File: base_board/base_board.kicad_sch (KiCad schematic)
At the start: 53 parts, among them J1 Conn_ARM_JTAG_SWD_20, SW1 SW_Push, U1 STM32F446ZEJx, U2 IS42S16400J-xT, U3 BMI270, U4 USB_C_Receptacle_USB2.0, U5 10p, U6 10p, U7 LD3985M33R_SOT23, Y1 Crystal_GND24

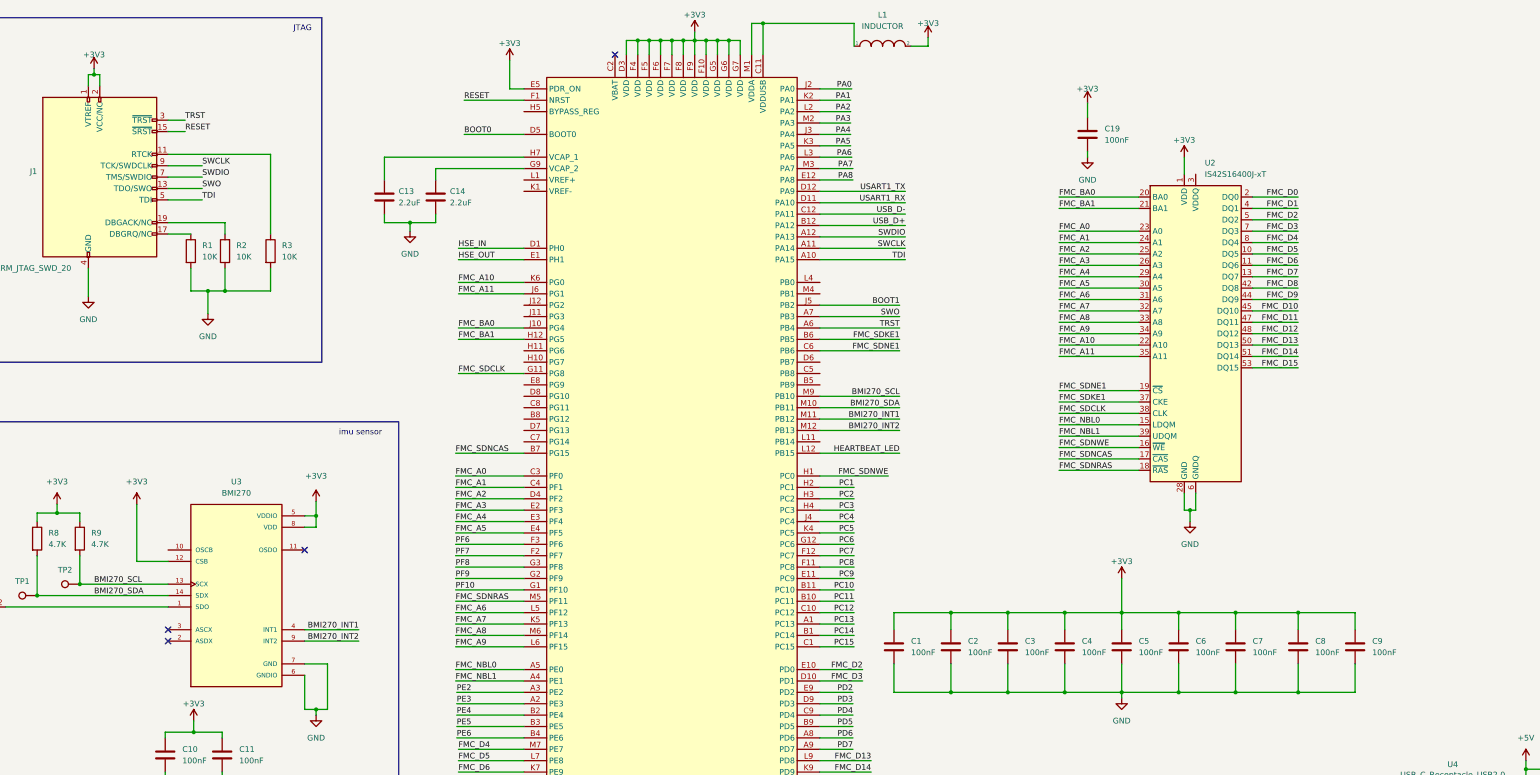
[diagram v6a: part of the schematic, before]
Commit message: [pcb] completed routing except VDDUSB
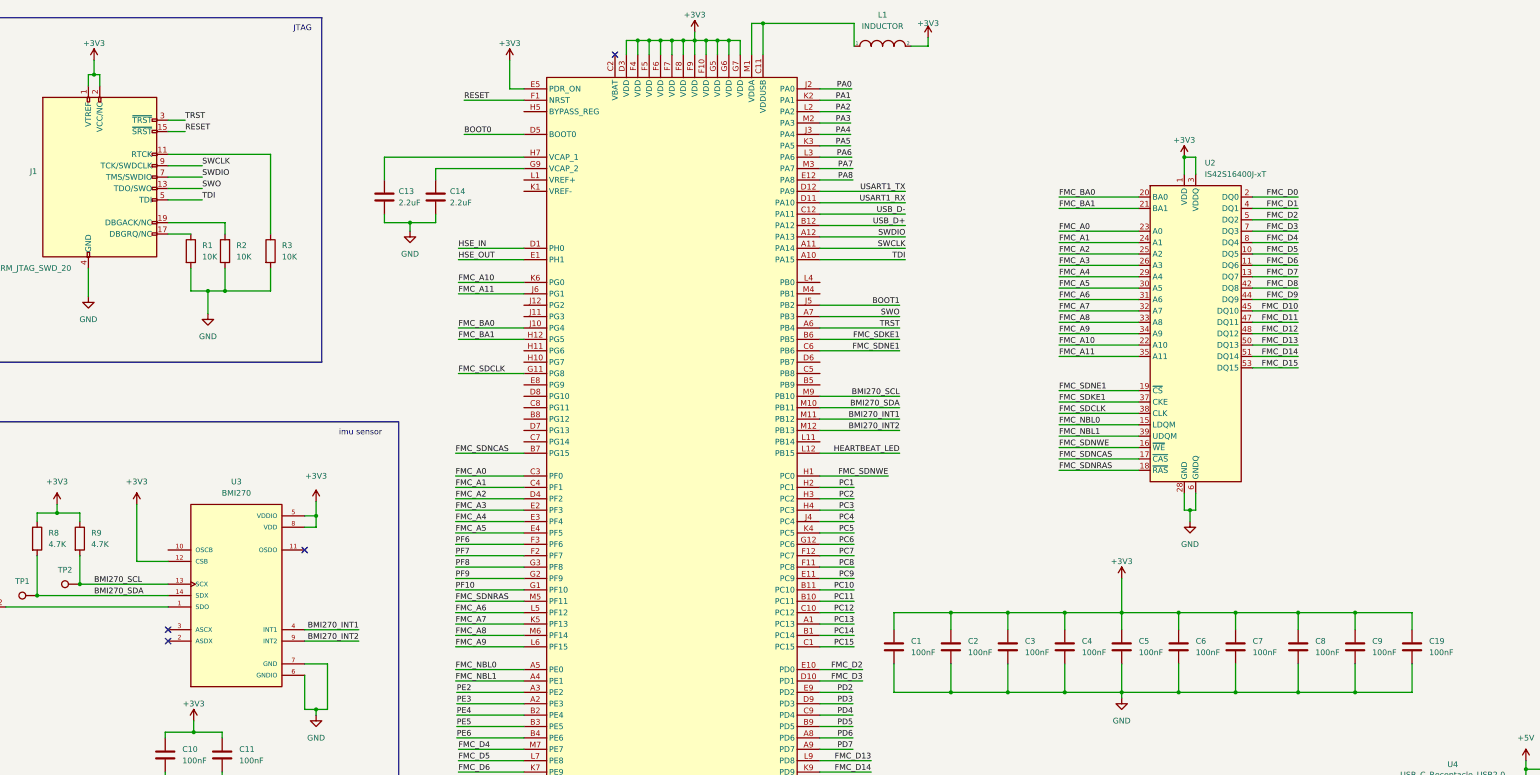
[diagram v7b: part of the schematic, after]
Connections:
- net +3.3V is gone; now on net +3V3: J1.1 (VTREF), J1.2 (VCC/NC)
- net +3V3: now also U2.3 (VDDQ), U2.43 (VDDQ), U2.49 (VDDQ), U2.9 (VDDQ)
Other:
- moved on the sheet: C19
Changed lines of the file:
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@@
   (junction (at 58.42 255.905) (diameter 0) (color 0 0 0 0)
   )
+  (junction (at 323.85 165.1) (diameter 0) (color 0 0 0 0)
+  )
   (junction (at 361.95 182.245) (diameter 0) (color 0 0 0 0)
   )
@@
   (junction (at 297.18 147.32) (diameter 0) (color 0 0 0 0)
   )
+  (junction (at 323.85 147.32) (diameter 0) (color 0 0 0 0)
+  )
   (junction (at 259.08 165.1) (diameter 0) (color 0 0 0 0)
   )
@@
   (junction (at 179.07 209.55) (diameter 0) (color 0 0 0 0)
   )
+  (junction (at 285.75 45.72) (diameter 0) (color 0 0 0 0)
+  )
   (junction (at 175.26 209.55) (diameter 0) (color 0 0 0 0)
   )
@@
     (stroke (width 0) (type default))
   )
+  (wire (pts (xy 336.55 147.32) (xy 323.85 147.32))
+    (stroke (width 0) (type default))
+  )
   (wire (pts (xy 259.08 147.32) (xy 246.38 147.32))
     (stroke (width 0) (type default))
@@
     (stroke (width 0) (type default))
   )
+  (wire (pts (xy 288.29 49.53) (xy 288.29 45.72))
+    (stroke (width 0) (type default))
+  )
   (wire (pts (xy 259.08 165.1) (xy 271.78 165.1))
     (stroke (width 0) (type default))
@@
     (stroke (width 0) (type default))
   )
+  (wire (pts (xy 336.55 165.1) (xy 323.85 165.1))
+    (stroke (width 0) (type default))
+  )
   (wire (pts (xy 123.19 132.08) (xy 138.43 132.08))
     (stroke (width 0) (type default))
@@
     (stroke (width 0) (type default))
   )
-  (wire (pts (xy 42.545 26.035) (xy 42.545 27.305))
+  (wire (pts (xy 42.545 24.13) (xy 42.545 27.305))
     (stroke (width 0) (type default))
   )
@@
     (stroke (width 0) (type default))
   )
+  (wire (pts (xy 336.55 151.13) (xy 336.55 147.32))
+    (stroke (width 0) (type default))
+  )
   (wire (pts (xy 89.535 128.27) (xy 92.075 128.27))
     (stroke (width 0) (type default))
@@
     (stroke (width 0) (type default))
   )
-  (wire (pts (xy 264.16 44.45) (xy 264.16 45.72))
-    (stroke (width 0) (type default))
-  )
   (wire (pts (xy 181.61 209.55) (xy 184.15 209.55))
     (stroke (width 0) (type default))
@@
     (stroke (width 0) (type default))
   )
+  (wire (pts (xy 336.55 158.75) (xy 336.55 165.1))
+    (stroke (width 0) (type default))
+  )
   (wire (pts (xy 300.99 59.69) (xy 311.15 59.69))
     (stroke (width 0) (type default))
@@
     (stroke (width 0) (type default))
   )
-  (wire (pts (xy 264.16 33.655) (xy 264.16 36.83))
-    (stroke (width 0) (type default))
-  )
   (wire (pts (xy 52.07 123.19) (xy 52.07 135.89))
     (stroke (width 0) (type default))
@@
     (stroke (width 0) (type default))
   )
+  (wire (pts (xy 285.75 45.72) (xy 288.29 45.72))
+    (stroke (width 0) (type default))
+  )
   (wire (pts (xy 204.47 88.9) (xy 222.25 88.9))
     (stroke (width 0) (type default))
@@
     )
   )
+  (symbol (lib_name "+3V3_7") (lib_id "power:+3V3") (at 42.545 24.13 0) (unit 1)
+    (in_bom yes) (on_board yes) (dnp no) (fields_autoplaced)
+    (property "Reference" "#PWR06" (at 42.545 27.94 0)
+      (effects (font (size 1.27 1.27)) hide)
+    )
+    (property "Value" "+3V3" (at 42.545 20.32 0)
+      (effects (font (size 1.27 1.27)))
+    )
+    (property "Footprint" "" (at 42.545 24.13 0)
+      (effects (font (size 1.27 1.27)) hide)
+    )
+    (property "Datasheet" "" (at 42.545 24.13 0)
+      (effects (font (size 1.27 1.27)) hide)
+    )
+    (pin "1")
+    (instances
+      (project "base_board"
+        (path "/2307506f-1d7e-4fdb-b101-b9905788fe29"
+          (reference "#PWR06") (unit 1)
+        )
+      )
+    )
+  )
   (symbol (lib_id "Device:R") (at 64.135 66.675 0) (unit 1)
     (in_bom yes) (on_board yes) (dnp no) (fields_autoplaced)
@@
     )
   )
-  (symbol (lib_id "power:+3.3V") (at 42.545 26.035 0) (unit 1)
-    (in_bom yes) (on_board yes) (dnp no) (fields_autoplaced)
-    (property "Reference" "#PWR0103" (at 42.545 29.845 0)
-      (effects (font (size 1.27 1.27)) hide)
-    )
-    (property "Value" "+3V3" (at 42.545 22.86 0)
-      (effects (font (size 1.27 1.27)))
-    )
-    (property "Footprint" "" (at 42.545 26.035 0)
-      (effects (font (size 1.27 1.27)) hide)
-    )
-    (property "Datasheet" "" (at 42.545 26.035 0)
-      (effects (font (size 1.27 1.27)) hide)
-    )
-    (pin "1")
-    (instances
-      (project "base_board"
-        (path "/2307506f-1d7e-4fdb-b101-b9905788fe29"
-          (reference "#PWR0103") (unit 1)
-        )
-      )
-    )
-  )
   (symbol (lib_id "Device:C") (at 27.94 222.885 0) (unit 1)
     (in_bom yes) (on_board yes) (dnp no) (fields_autoplaced)
@@
     )
   )
-  (symbol (lib_name "+3V3_6") (lib_id "power:+3V3") (at 264.16 33.655 0) (unit 1)
-    (in_bom yes) (on_board yes) (dnp no) (fields_autoplaced)
-    (property "Reference" "#PWR06" (at 264.16 37.465 0)
-      (effects (font (size 1.27 1.27)) hide)
-    )
-    (property "Value" "+3V3" (at 264.16 30.48 0)
-      (effects (font (size 1.27 1.27)))
-    )
-    (property "Footprint" "" (at 264.16 33.655 0)
-      (effects (font (size 1.27 1.27)) hide)
-    )
-    (property "Datasheet" "" (at 264.16 33.655 0)
-      (effects (font (size 1.27 1.27)) hide)
-    )
-    (pin "1")
-    (instances
-      (project "base_board"
-        (path "/2307506f-1d7e-4fdb-b101-b9905788fe29"
-          (reference "#PWR06") (unit 1)
-        )
-      )
-    )
-  )
   (symbol (lib_id "power:+3V3") (at 58.42 245.745 0) (unit 1)
     (in_bom yes) (on_board yes) (dnp no) (fields_autoplaced)
@@
     )
   )
-  (symbol (lib_name "GND_1") (lib_id "power:GND") (at 264.16 45.72 0) (mirror y) (unit 1)
-    (in_bom yes) (on_board yes) (dnp no)
-    (property "Reference" "#PWR07" (at 264.16 52.07 0)
-      (effects (font (size 1.27 1.27)) hide)
-    )
-    (property "Value" "GND" (at 264.16 50.8 0)
-      (effects (font (size 1.27 1.27)))
-    )
-    (property "Footprint" "" (at 264.16 45.72 0)
-      (effects (font (size 1.27 1.27)) hide)
-    )
-    (property "Datasheet" "" (at 264.16 45.72 0)
-      (effects (font (size 1.27 1.27)) hide)
-    )
-    (pin "1")
-    (instances
-      (project "base_board"
-        (path "/2307506f-1d7e-4fdb-b101-b9905788fe29"
-          (reference "#PWR07") (unit 1)
-        )
-      )
-    )
-  )
   (symbol (lib_id "power:+3V3") (at 250.19 252.095 0) (unit 1)
     (in_bom yes) (on_board yes) (dnp no) (fields_autoplaced)
@@
     )
   )
-  (symbol (lib_id "Device:C") (at 264.16 40.64 0) (unit 1)
+  (symbol (lib_id "Device:C") (at 336.55 154.94 0) (unit 1)
     (in_bom yes) (on_board yes) (dnp no) (fields_autoplaced)
-    (property "Reference" "C19" (at 267.97 39.3699 0)
+    (property "Reference" "C19" (at 340.36 153.6699 0)
       (effects (font (size 1.27 1.27)) (justify left))
     )
-    (property "Value" "100nF" (at 267.97 41.9099 0)
+    (property "Value" "100nF" (at 340.36 156.2099 0)
       (effects (font (size 1.27 1.27)) (justify left))
     )
-    (property "Footprint" "Capacitor_SMD:C_0603_1608Metric" (at 265.1252 44.45 0)
+    (property "Footprint" "Capacitor_SMD:C_0603_1608Metric" (at 337.5152 158.75 0)
       (effects (font (size 1.27 1.27)) hide)
     )
-    (property "Datasheet" "~" (at 264.16 40.64 0)
+    (property "Datasheet" "~" (at 336.55 154.94 0)
       (effects (font (size 1.27 1.27)) hide)
     )

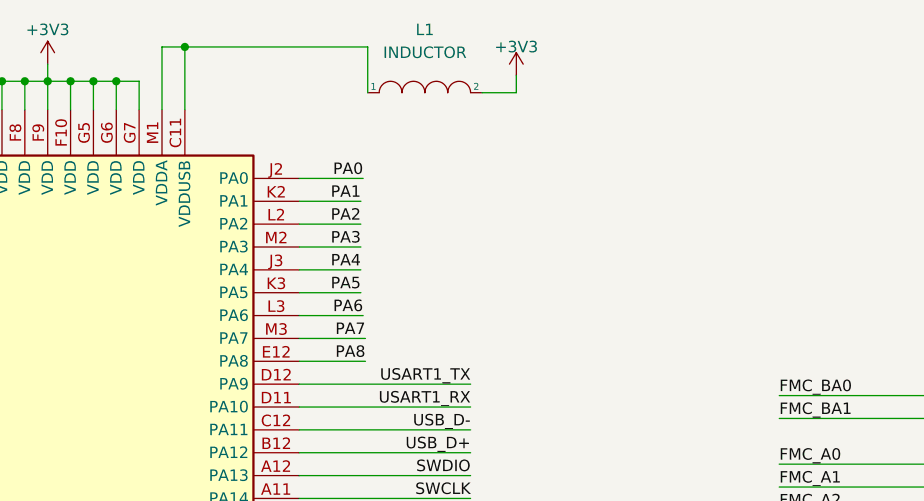
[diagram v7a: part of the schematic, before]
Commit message: [pcb] added caps for VDDUSB
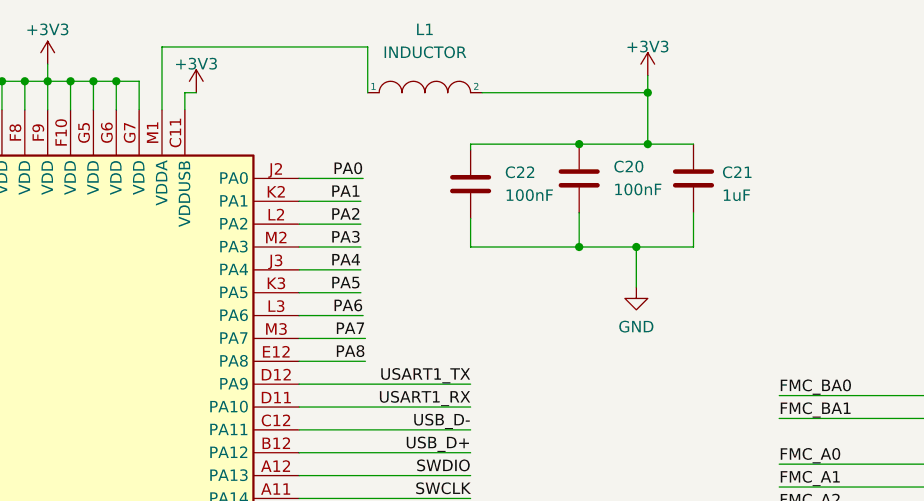
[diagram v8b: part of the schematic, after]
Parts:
- added C20, C22: 100nF, Capacitor_SMD:C_0603_1608Metric, symbol Device:C
- added C21: 1uF, Capacitor_SMD:C_0603_1608Metric, symbol Device:C
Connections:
- net +3V3: now also U1.C11 (VDDUSB), C20.1, C21.1, C22.1
- net GND: now also C20.2, C21.2, C22.2
- net at L1.1, U1.M1 (VDDA): no longer U1.C11 (VDDUSB)
